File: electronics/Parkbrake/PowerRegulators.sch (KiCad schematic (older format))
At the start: 23 parts, among them U21 MIC2619, U22 MC34063, U23 LD1117S33CTR

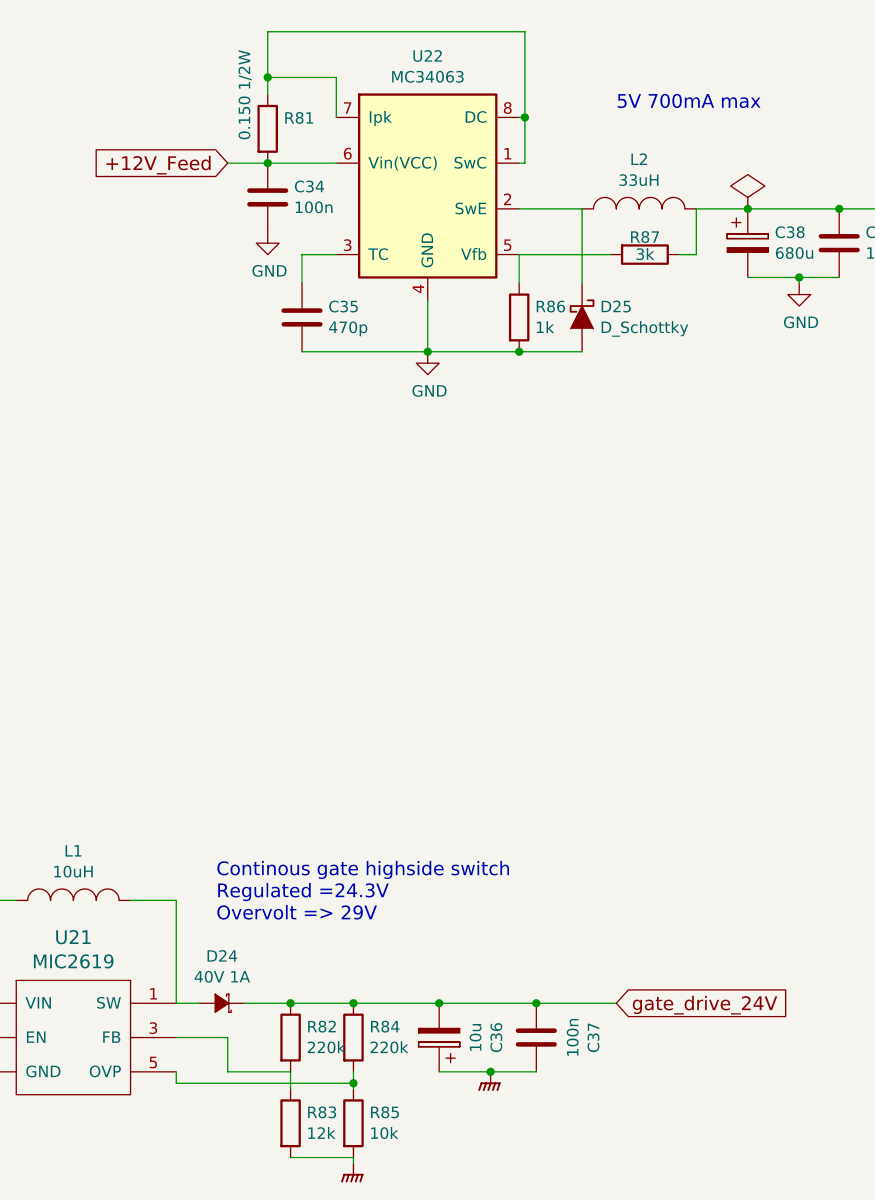
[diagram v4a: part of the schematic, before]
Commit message: More fixes and chenged components eat less boardspace
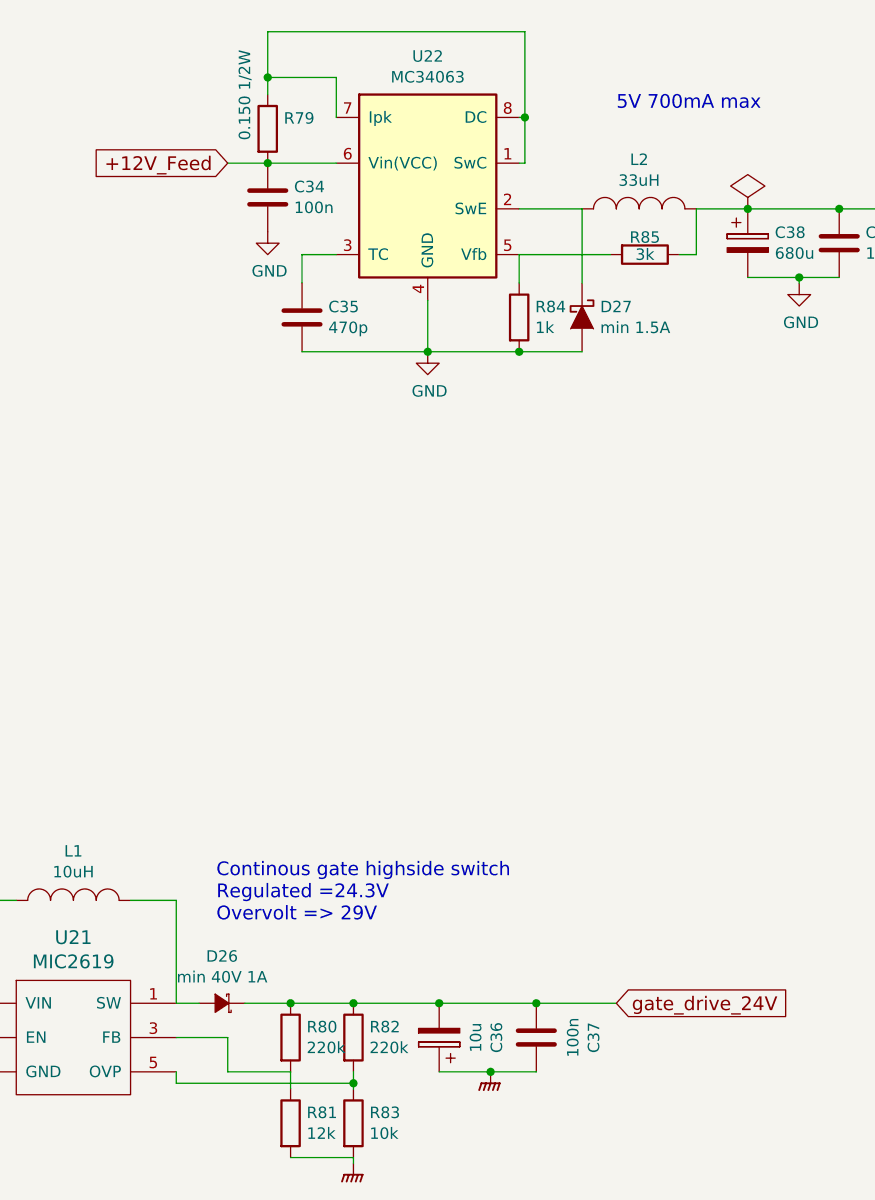
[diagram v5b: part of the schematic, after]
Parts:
- C36: footprint Capacitors_SMD:c_elec_5x5.3 -> Capacitors_Tantalum_SMD:TantalC_SizeC_EIA-6032_Wave; farnell 1870621 -> 1457464; part MCESL35V106M5X5.2 -> T491C106K035AT
- C38: footprint Capacitors_SMD:c_elec_10x10.5 -> Capacitors_Tantalum_SMD:TantalC_SizeD_EIA-7343_Wave; farnell 2507731 -> 2283882; part EEEFK1E681SP -> TPSE687K006R0060
- C40, C41: footprint Capacitors_SMD:c_elec_5x5.3 -> myfootprints:CP_0805; farnell 1870621 -> 2491430; part MCESL35V106M5X5.2 -> TMCP0J106KTRF
- D26: renamed from D24; value 40V 1A -> min 40V 1A; footprint Diodes_SMD:DO-214AB -> Diodes_SMD:SOD-123; farnell 2353680 -> 2473419; part STPS3L40S -> NTS260SFT1G
- D27: renamed from D25; value D_Schottky -> min 1.5A; footprint Diodes_SMD:DO-214AB -> Diodes_SMD:SOD-123; farnell 2353680 -> 2473419; part STPS3L40S -> NTS260SFT1G
- L1: footprint Inductors:Inductor_1212 -> myfootprints:inductor_sd54
- L2: footprint Inductors:SELF-WE-PD-XXL -> myfootprints:inductor_sd54; farnell 2374128 -> 2526983; part SRR1260A-330M -> SD54-333MLB
- R83: renamed from R85; farnell (none) -> 9332391; part 9332391 -> MC01W0805110K
- renumbered R81 to R79, R82 to R80, R83 to R81, R84 to R82, R86 to R84, R87 to R85
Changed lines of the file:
@@
 F 0 "L1" H 2125 5765 50  0000 C CNN
 F 1 "10uH" H 2125 5674 50  0000 C CNN
-F 2 "Inductors:Inductor_1212" H 2125 5550 50  0001 C CNN
+F 2 "myfootprints:inductor_sd54" H 2125 5550 50  0001 C CNN
 F 3 "" H 2125 5550 50  0000 C CNN
 F 4 "LQH32CN100K33L" H 2125 5550 60  0001 C CNN "part"
@@
 F 0 "C36" V 3473 6150 50  0000 C CNN
 F 1 "10u" V 3564 6150 50  0000 C CNN
-F 2 "Capacitors_SMD:c_elec_5x5.3" H 3763 6000 50  0001 C CNN
+F 2 "Capacitors_Tantalum_SMD:TantalC_SizeC_EIA-6032_Wave" H 3763 6000 50  0001 C CNN
 F 3 "" H 3725 6150 50  0000 C CNN
-F 4 "MCESL35V106M5X5.2" V 3725 6150 60  0001 C CNN "part"
-F 5 "1870621" V 3725 6150 60  0001 C CNN "farnell"
+F 4 "T491C106K035AT" V 3725 6150 60  0001 C CNN "part"
+F 5 "1457464" V 3725 6150 60  0001 C CNN "farnell"
 	1    3725 6150
 	-1   0    0    1
 $EndComp
 $Comp
-L GNDPWR #PWR064
+L GNDPWR #PWR59
 U 1 1 57010C16
 P 1675 6425
-F 0 "#PWR064" H 1675 6225 50  0001 C CNN
+F 0 "#PWR59" H 1675 6225 50  0001 C CNN
 F 1 "GNDPWR" H 1675 6200 50  0001 C CNN
 F 2 "" H 1675 6375 50  0000 C CNN
@@
 $EndComp
 $Comp
-L D_Schottky_Small D24
+L D_Schottky_Small D26
 U 1 1 57010E55
 P 2775 6000
-F 0 "D24" H 2775 5795 50  0000 C CNN
-F 1 "40V 1A" H 2775 5886 50  0000 C CNN
-F 2 "Diodes_SMD:DO-214AB" V 2775 6000 50  0001 C CNN
+F 0 "D26" H 2775 5795 50  0000 C CNN
+F 1 "min 40V 1A" H 2775 5886 50  0000 C CNN
+F 2 "Diodes_SMD:SOD-123" V 2775 6000 50  0001 C CNN
 F 3 "" V 2775 6000 50  0000 C CNN
-F 4 "STPS3L40S" H 2775 6000 60  0001 C CNN "part"
-F 5 "2353680" H 2775 6000 60  0001 C CNN "farnell"
+F 4 "NTS260SFT1G" H 2775 6000 60  0001 C CNN "part"
+F 5 "2473419" H 2775 6000 60  0001 C CNN "farnell"
 	1    2775 6000
 	-1   0    0    1
 $EndComp
 $Comp
-L R R82
+L R R80
 U 1 1 57010F19
 P 3075 6150
-F 0 "R82" H 3145 6196 50  0000 L CNN
+F 0 "R80" H 3145 6196 50  0000 L CNN
 F 1 "220k" H 3145 6105 50  0000 L CNN
 F 2 "Resistors_SMD:R_0805" V 3005 6150 50  0001 C CNN
@@
 $EndComp
 $Comp
-L R R83
+L R R81
 U 1 1 57010F4F
 P 3075 6525
-F 0 "R83" H 3145 6571 50  0000 L CNN
+F 0 "R81" H 3145 6571 50  0000 L CNN
 F 1 "12k" H 3145 6480 50  0000 L CNN
 F 2 "Resistors_SMD:R_0805" V 3005 6525 50  0001 C CNN
@@
 $EndComp
 $Comp
-L R R84
+L R R82
 U 1 1 57011141
 P 3350 6150
-F 0 "R84" H 3420 6196 50  0000 L CNN
+F 0 "R82" H 3420 6196 50  0000 L CNN
 F 1 "220k" H 3420 6105 50  0000 L CNN
 F 2 "Resistors_SMD:R_0805" V 3280 6150 50  0001 C CNN
@@
 $EndComp
 $Comp
-L R R85
+L R R83
 U 1 1 57011177
 P 3350 6525
-F 0 "R85" H 3420 6571 50  0000 L CNN
+F 0 "R83" H 3420 6571 50  0000 L CNN
 F 1 "10k" H 3420 6480 50  0000 L CNN
 F 2 "Resistors_SMD:R_0805" V 3280 6525 50  0001 C CNN
 F 3 "" H 3350 6525 50  0000 C CNN
 F 4 "MC01W0805110K" H 3350 6525 60  0001 C CNN "part"
-F 5 "9332391" H 3350 6525 60  0001 C CNN "part"
+F 5 "9332391" H 3350 6525 60  0001 C CNN "farnell"
 	1    3350 6525
 	1    0    0    -1
 $EndComp
 $Comp
-L GNDPWR #PWR065
+L GNDPWR #PWR61
 U 1 1 57011519
 P 3350 6700
-F 0 "#PWR065" H 3350 6500 50  0001 C CNN
+F 0 "#PWR61" H 3350 6500 50  0001 C CNN
 F 1 "GNDPWR" H 3357 6774 50  0001 C CNN
 F 2 "" H 3350 6650 50  0000 C CNN
@@
 $EndComp
 $Comp
-L GNDPWR #PWR066
+L GNDPWR #PWR63
 U 1 1 57011573
 P 3950 6300
-F 0 "#PWR066" H 3950 6100 50  0001 C CNN
+F 0 "#PWR63" H 3950 6100 50  0001 C CNN
 F 1 "GNDPWR" H 3957 6374 50  0001 C CNN
 F 2 "" H 3950 6250 50  0000 C CNN
@@
 gate_drive_24V
 $Comp
-L MC34063-RESCUE-Parkbrake U?
+L MC34063-RESCUE-Parkbrake U22
 U 1 1 57089F7E
 P 3675 2425
-AR Path="/57089F7E" Ref="U?"  Part="1"
-AR Path="/57088F10/57089F7E" Ref="U22"  Part="1"
 F 0 "U22" H 3675 2992 50  0000 C CNN
 F 1 "MC34063" H 3675 2901 50  0000 C CNN
@@
 $EndComp
 $Comp
-L GND #PWR067
+L GND #PWR62
 U 1 1 5708A002
 P 3675 3150
-F 0 "#PWR067" H 3675 2900 50  0001 C CNN
+F 0 "#PWR62" H 3675 2900 50  0001 C CNN
 F 1 "GND" H 3683 2977 50  0000 C CNN
 F 2 "" H 3675 3150 50  0000 C CNN
@@
 $EndComp
 $Comp
-L R R86
+L R R84
 U 1 1 5708A132
 P 4075 3000
-F 0 "R86" H 4145 3046 50  0000 L CNN
+F 0 "R84" H 4145 3046 50  0000 L CNN
 F 1 "1k" H 4145 2955 50  0000 L CNN
 F 2 "Resistors_SMD:R_0805" V 4005 3000 50  0001 C CNN
@@
 $EndComp
 $Comp
-L R R87
+L R R85
 U 1 1 5708A176
 P 4625 2725
-F 0 "R87" V 4550 2725 50  0000 C CNN
+F 0 "R85" V 4550 2725 50  0000 C CNN
 F 1 "3k" V 4625 2725 50  0000 C CNN
 F 2 "Resistors_SMD:R_0805" V 4555 2725 50  0001 C CNN
@@
 $EndComp
 $Comp
-L R R81
+L R R79
 U 1 1 5708A1CB
 P 2975 2175
-F 0 "R81" H 3045 2221 50  0000 L CNN
+F 0 "R79" H 3045 2221 50  0000 L CNN
 F 1 "0.150 1/2W" V 2875 2125 50  0000 L CNN
 F 2 "Resistors_SMD:R_1206" V 2905 2175 50  0001 C CNN
@@
 F 0 "L2" H 4600 2740 50  0000 C CNN
 F 1 "33uH" H 4600 2649 50  0000 C CNN
-F 2 "Inductors:SELF-WE-PD-XXL" H 4600 2525 50  0001 C CNN
+F 2 "myfootprints:inductor_sd54" H 4600 2525 50  0001 C CNN
 F 3 "" H 4600 2525 50  0000 C CNN
-F 4 "SRR1260A-330M" H 4600 2525 60  0001 C CNN "part"
-F 5 "2374128" H 4600 2525 60  0001 C CNN "farnell"
+F 4 "SD54-333MLB" H 4600 2525 60  0001 C CNN "part"
+F 5 "2526983" H 4600 2525 60  0001 C CNN "farnell"
 	1    4600 2525
 	1    0    0    -1
 $EndComp
 $Comp
-L D_Schottky D25
+L D_Schottky D27
 U 1 1 5708A2E4
 P 4350 3000
-F 0 "D25" V 4304 3079 50  0000 L CNN
-F 1 "D_Schottky" V 4395 3079 50  0000 L CNN
-F 2 "Diodes_SMD:DO-214AB" H 4350 3000 50  0001 C CNN
+F 0 "D27" V 4304 3079 50  0000 L CNN
+F 1 "min 1.5A" V 4395 3079 50  0000 L CNN
+F 2 "Diodes_SMD:SOD-123" H 4350 3000 50  0001 C CNN
 F 3 "" H 4350 3000 50  0000 C CNN
-F 4 "STPS3L40S" V 4350 3000 60  0001 C CNN "part"
-F 5 "2353680" V 4350 3000 60  0001 C CNN "farnell"
+F 4 "NTS260SFT1G" V 4350 3000 60  0001 C CNN "part"
+F 5 "2473419" V 4350 3000 60  0001 C CNN "farnell"
 	1    4350 3000
 	0    1    1    0
@@
 F 0 "C38" H 5193 2721 50  0000 L CNN
 F 1 "680u" H 5193 2630 50  0000 L CNN
-F 2 "Capacitors_SMD:c_elec_10x10.5" H 5113 2525 50  0001 C CNN
+F 2 "Capacitors_Tantalum_SMD:TantalC_SizeD_EIA-7343_Wave" H 5113 2525 50  0001 C CNN
 F 3 "" H 5075 2675 50  0000 C CNN
-F 4 "EEEFK1E681SP" H 5075 2675 60  0001 C CNN "part"
-F 5 "2507731" H 5075 2675 60  0001 C CNN "farnell"
+F 4 "TPSE687K006R0060" H 5075 2675 60  0001 C CNN "part"
+F 5 "2283882" H 5075 2675 60  0001 C CNN "farnell"
 	1    5075 2675
 	1    0    0    -1
 $EndComp
 $Comp
-L GND #PWR068
+L GND #PWR64
 U 1 1 5708ABA3
 P 5300 2850
-F 0 "#PWR068" H 5300 2600 50  0001 C CNN
+F 0 "#PWR64" H 5300 2600 50  0001 C CNN
 F 1 "GND" H 5308 2677 50  0000 C CNN
 F 2 "" H 5300 2850 50  0000 C CNN
@@
 $EndComp
 $Comp
-L GND #PWR069
+L GND #PWR60
 U 1 1 5708B974
 P 2975 2625
-F 0 "#PWR069" H 2975 2375 50  0001 C CNN
+F 0 "#PWR60" H 2975 2375 50  0001 C CNN
 F 1 "GND" H 2983 2452 50  0000 C CNN
 F 2 "" H 2975 2625 50  0000 C CNN
@@
 F 0 "C40" H 7990 2496 50  0000 L CNN
 F 1 "10u" H 7990 2405 50  0000 L CNN
-F 2 "Capacitors_SMD:c_elec_5x5.3" H 7913 2300 50  0001 C CNN
+F 2 "myfootprints:CP_0805" H 7913 2300 50  0001 C CNN
 F 3 "" H 7875 2450 50  0000 C CNN
-F 4 "MCESL35V106M5X5.2" H 7875 2450 60  0001 C CNN "part"
-F 5 "1870621" H 7875 2450 60  0001 C CNN "farnell"
+F 4 "TMCP0J106KTRF" H 7875 2450 60  0001 C CNN "part"
+F 5 "2491430" H 7875 2450 60  0001 C CNN "farnell"
 	1    7875 2450
 	1    0    0    -1
@@
 F 0 "C41" H 9140 2496 50  0000 L CNN
 F 1 "10u" H 9140 2405 50  0000 L CNN
-F 2 "Capacitors_SMD:c_elec_5x5.3" H 9063 2300 50  0001 C CNN
+F 2 "myfootprints:CP_0805" H 9063 2300 50  0001 C CNN
 F 3 "" H 9025 2450 50  0000 C CNN
-F 4 "MCESL35V106M5X5.2" H 9025 2450 60  0001 C CNN "part"
-F 5 "1870621" H 9025 2450 60  0001 C CNN "farnell"
+F 4 "TMCP0J106KTRF" H 9025 2450 60  0001 C CNN "part"
+F 5 "2491430" H 9025 2450 60  0001 C CNN "farnell"
 	1    9025 2450
 	1    0    0    -1
 $EndComp
 $Comp
-L GND #PWR070
+L GND #PWR65
 U 1 1 5708D552
 P 8450 2775
-F 0 "#PWR070" H 8450 2525 50  0001 C CNN
+F 0 "#PWR65" H 8450 2525 50  0001 C CNN
 F 1 "GND" H 8458 2602 50  0000 C CNN
 F 2 "" H 8450 2775 50  0000 C CNN
@@
 +3.3V
 $Comp
-L PWR_FLAG #FLG071
+L PWR_FLAG #FLG12
 U 1 1 57980F2B
 P 9025 2300
-F 0 "#FLG071" H 9025 2395 50  0001 C CNN
+F 0 "#FLG12" H 9025 2395 50  0001 C CNN
 F 1 "PWR_FLAG" H 9025 2480 50  0001 C CNN
 F 2 "" H 9025 2300 50  0000 C CNN
@@
 $EndComp
 $Comp
-L PWR_FLAG #FLG072
+L PWR_FLAG #FLG11
 U 1 1 5798551D
 P 5075 2525
-F 0 "#FLG072" H 5075 2620 50  0001 C CNN
+F 0 "#FLG11" H 5075 2620 50  0001 C CNN
 F 1 "PWR_FLAG" H 5075 2705 50  0001 C CNN
 F 2 "" H 5075 2525 50  0000 C CNN
